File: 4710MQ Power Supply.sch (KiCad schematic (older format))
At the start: 20 parts, among them J1 Jack-DC, J2 ATX 4 Pin, J3 Molex 4 Pin, U1 MP1499GD-Z

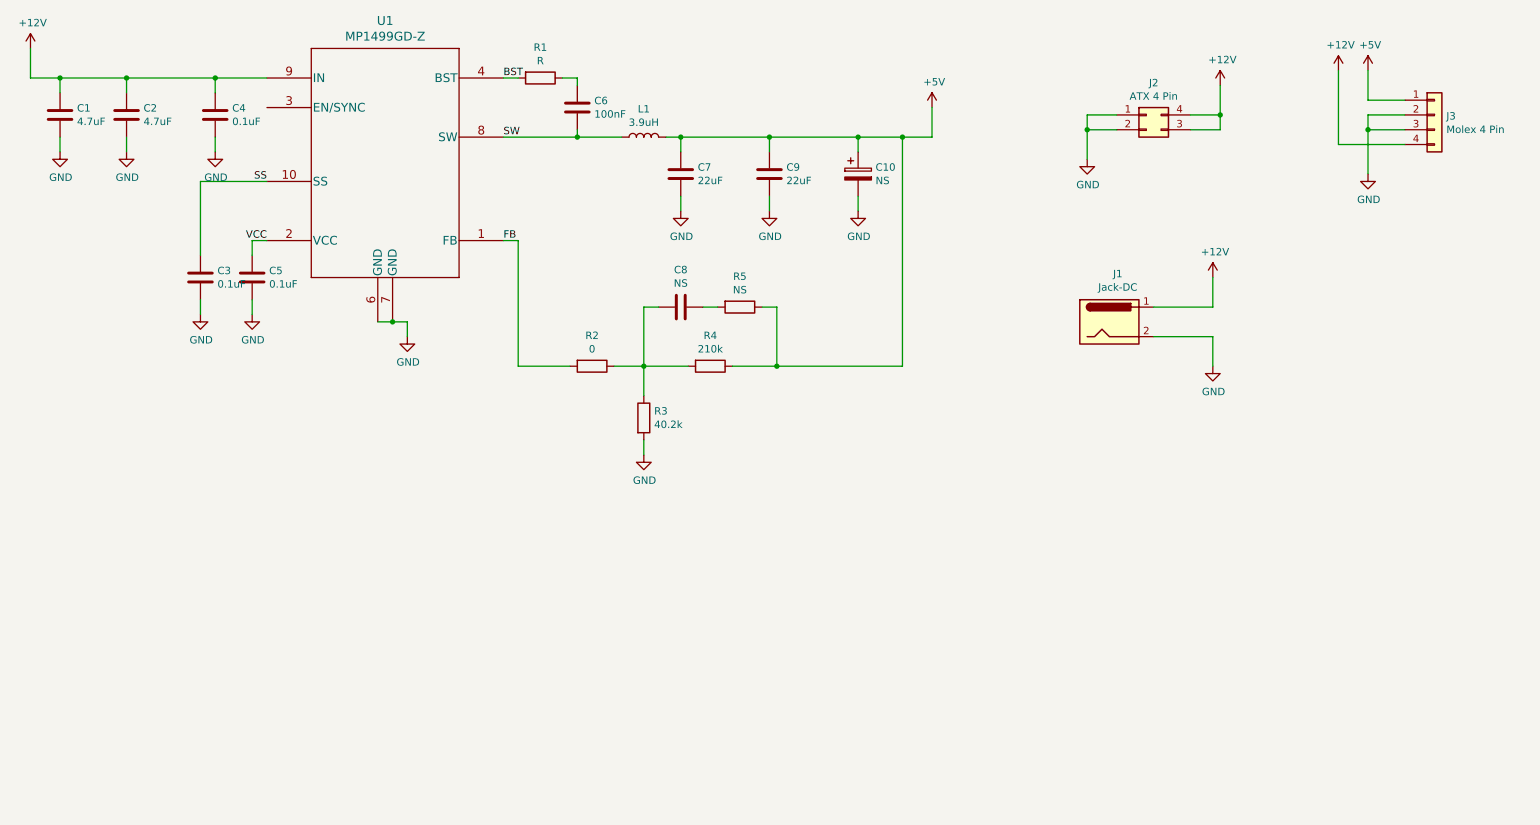
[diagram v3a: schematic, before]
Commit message: Version 3.0
- Added Current Sensor
- Added Thermometer IC
- Added 2.54 pitch 4pin output
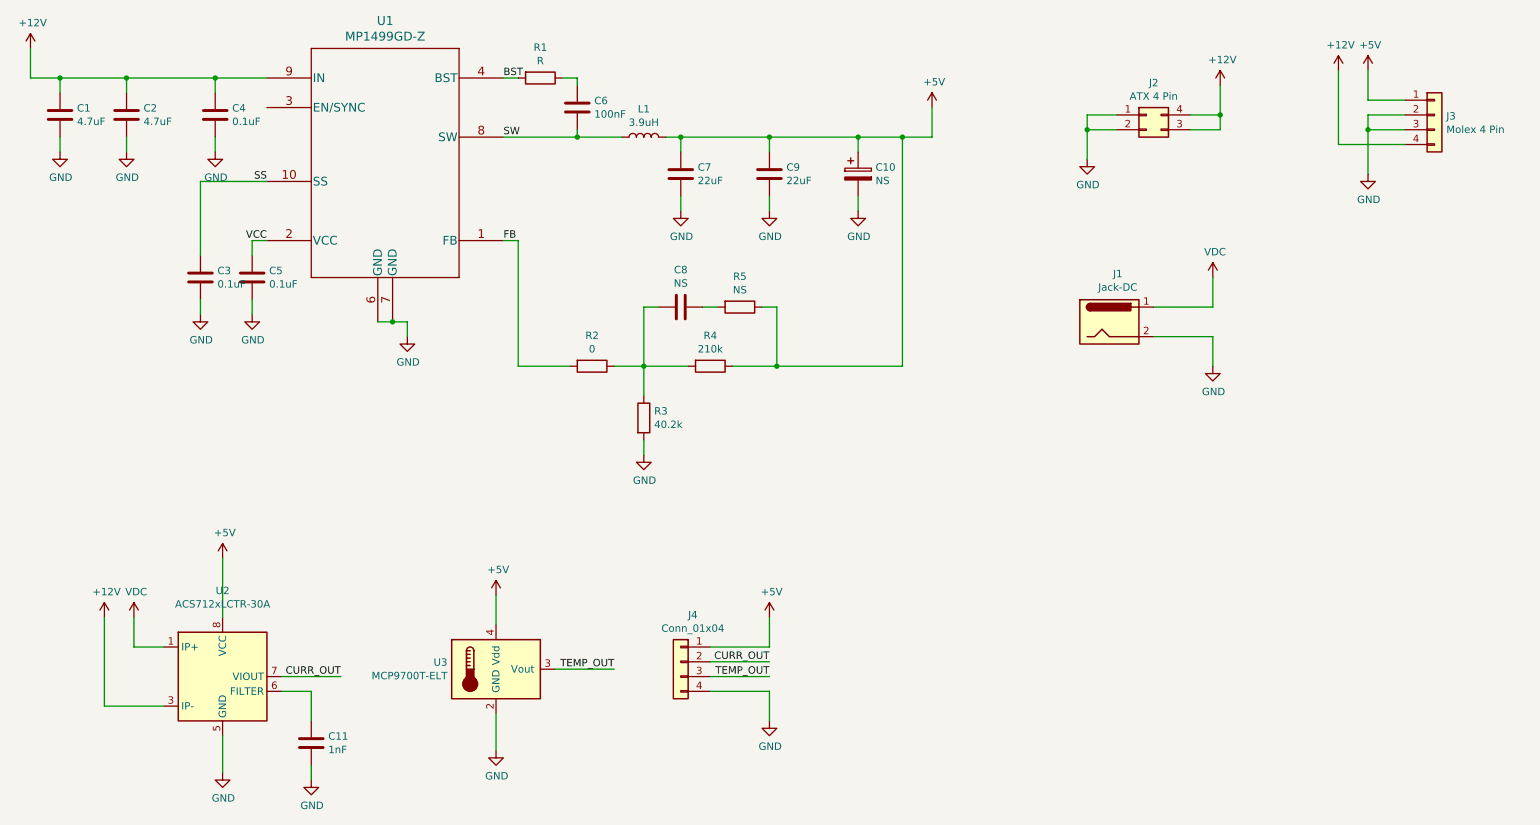
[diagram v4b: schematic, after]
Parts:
- added C11: 1nF, Capacitor_SMD:C_0805_2012Metric_Pad1.18x1.45mm_HandSolder, symbol Device:C
- added J4: Conn_01x04, Connector_PinSocket_2.54mm:PinSocket_1x04_P2.54mm_Vertical, symbol Connector_Generic:Conn_01x04
- added U2: ACS712xLCTR-30A, Package_SO:SOIC-8_3.9x4.9mm_P1.27mm, symbol Sensor_Current:ACS712xLCTR-30A
- added U3: MCP9700T-ELT, Package_TO_SOT_SMD:SOT-353_SC-70-5, symbol Sensor_Temperature:MCP9700T-ELT
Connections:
- net +12V: now also U2.3 (IP-), U2.4 (IP-); no longer J1.1
- net +5V: now also J4.1 (Pin_1), U2.8 (VCC), U3.4 (Vdd)
- net GND: now also C11.2, J4.4 (Pin_4), U2.5 (GND), U3.2 (GND)
- new net: C11.1, U2.6 (FILTER)
- new net CURR_OUT: J4.2 (Pin_2), U2.7 (VIOUT)
- new net TEMP_OUT: J4.3 (Pin_3), U3.3 (Vout)
- new net VDC: J1.1, U2.1 (IP+), U2.2 (IP+)
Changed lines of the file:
@@
 $EndComp
 $Comp
-L power:+12V #PWR0101
-U 1 1 614C8ABC
-P 8700 2550
-F 0 "#PWR0101" H 8700 2400 50  0001 C CNN
-F 1 "+12V" H 8715 2723 50  0000 C CNN
-F 2 "" H 8700 2550 50  0001 C CNN
-F 3 "" H 8700 2550 50  0001 C CNN
-	1    8700 2550
-	1    0    0    -1
-$EndComp
-$Comp
-L power:GND #PWR?
+L power:GND #PWR0101
 U 1 1 614CA392
 P 4850 3750
-F 0 "#PWR?" H 4850 3500 50  0001 C CNN
+F 0 "#PWR0101" H 4850 3500 50  0001 C CNN
 F 1 "GND" H 4855 3577 50  0000 C CNN
 F 2 "" H 4850 3750 50  0001 C CNN
@@
 	1    0    0    -1
 $EndComp
+$Comp
+L Sensor_Current:ACS712xLCTR-30A U2
+U 1 1 614D05D1
+P 2000 5250
+F 0 "U2" H 2000 5831 50  0000 C CNN
+F 1 "ACS712xLCTR-30A" H 2000 5740 50  0000 C CNN
+F 2 "Package_SO:SOIC-8_3.9x4.9mm_P1.27mm" H 2100 4900 50  0001 L CIN
+F 3 "http://www.allegromicro.com/~/media/Files/Datasheets/ACS712-Datasheet.ashx?la=en" H 2000 5250 50  0001 C CNN
+	1    2000 5250
+	1    0    0    -1
+$EndComp
+Wire Wire Line
+	1600 5050 1400 5050
+Wire Wire Line
+	1400 5050 1400 4850
+Wire Wire Line
+	1600 5450 1200 5450
+Wire Wire Line
+	1200 5450 1200 4850
+$Comp
+L power:+12V #PWR0102
+U 1 1 614D6643
+P 1200 4850
+F 0 "#PWR0102" H 1200 4700 50  0001 C CNN
+F 1 "+12V" H 1215 5023 50  0000 C CNN
+F 2 "" H 1200 4850 50  0001 C CNN
+F 3 "" H 1200 4850 50  0001 C CNN
+	1    1200 4850
+	1    0    0    -1
+$EndComp
+$Comp
+L power:VDC #PWR0103
+U 1 1 614D6B25
+P 1400 4850
+F 0 "#PWR0103" H 1400 4750 50  0001 C CNN
+F 1 "VDC" H 1415 5023 50  0000 C CNN
+F 2 "" H 1400 4850 50  0001 C CNN
+F 3 "" H 1400 4850 50  0001 C CNN
+	1    1400 4850
+	1    0    0    -1
+$EndComp
+$Comp
+L power:VDC #PWR0104
+U 1 1 614D6F1F
+P 8700 2550
+F 0 "#PWR0104" H 8700 2450 50  0001 C CNN
+F 1 "VDC" H 8715 2723 50  0000 C CNN
+F 2 "" H 8700 2550 50  0001 C CNN
+F 3 "" H 8700 2550 50  0001 C CNN
+	1    8700 2550
+	1    0    0    -1
+$EndComp
+Wire Wire Line
+	2000 4450 2000 4850
+$Comp
+L power:+5V #PWR0105
+U 1 1 614DC640
+P 2000 4450
+F 0 "#PWR0105" H 2000 4300 50  0001 C CNN
+F 1 "+5V" H 2015 4623 50  0000 C CNN
+F 2 "" H 2000 4450 50  0001 C CNN
+F 3 "" H 2000 4450 50  0001 C CNN
+	1    2000 4450
+	1    0    0    -1
+$EndComp
+Wire Wire Line
+	2000 5650 2000 5900
+$Comp
+L power:GND #PWR0106
+U 1 1 614DE695
+P 2000 5900
+F 0 "#PWR0106" H 2000 5650 50  0001 C CNN
+F 1 "GND" H 2005 5727 50  0000 C CNN
+F 2 "" H 2000 5900 50  0001 C CNN
+F 3 "" H 2000 5900 50  0001 C CNN
+	1    2000 5900
+	1    0    0    -1
+$EndComp
+Wire Wire Line
+	2400 5350 2600 5350
+Wire Wire Line
+	2600 5350 2600 5550
+$Comp
+L Device:C C11
+U 1 1 614E0AE1
+P 2600 5700
+F 0 "C11" H 2715 5746 50  0000 L CNN
+F 1 "1nF" H 2715 5655 50  0000 L CNN
+F 2 "Capacitor_SMD:C_0805_2012Metric_Pad1.18x1.45mm_HandSolder" H 2638 5550 50  0001 C CNN
+F 3 "~" H 2600 5700 50  0001 C CNN
+	1    2600 5700
+	1    0    0    -1
+$EndComp
+Wire Wire Line
+	2600 5850 2600 5950
+$Comp
+L power:GND #PWR0107
+U 1 1 614E305D
+P 2600 5950
+F 0 "#PWR0107" H 2600 5700 50  0001 C CNN
+F 1 "GND" H 2605 5777 50  0000 C CNN
+F 2 "" H 2600 5950 50  0001 C CNN
+F 3 "" H 2600 5950 50  0001 C CNN
+	1    2600 5950
+	1    0    0    -1
+$EndComp
+Wire Wire Line
+	2400 5250 2800 5250
+Text Label 2800 5250 2    50   ~ 0
+CURR_OUT
+Wire Wire Line
+	5300 5050 5700 5050
+Wire Wire Line
+	5300 5150 5700 5150
+Wire Wire Line
+	5300 5350 5700 5350
+Wire Wire Line
+	5700 5350 5700 5550
+Wire Wire Line
+	5700 5050 5700 4850
+Text Label 5700 5150 2    50   ~ 0
+CURR_OUT
+$Comp
+L power:+5V #PWR0108
+U 1 1 614F337E
+P 5700 4850
+F 0 "#PWR0108" H 5700 4700 50  0001 C CNN
+F 1 "+5V" H 5715 5023 50  0000 C CNN
+F 2 "" H 5700 4850 50  0001 C CNN
+F 3 "" H 5700 4850 50  0001 C CNN
+	1    5700 4850
+	1    0    0    -1
+$EndComp
+$Comp
+L power:GND #PWR0109
+U 1 1 614F382B
+P 5700 5550
+F 0 "#PWR0109" H 5700 5300 50  0001 C CNN
+F 1 "GND" H 5705 5377 50  0000 C CNN
+F 2 "" H 5700 5550 50  0001 C CNN
+F 3 "" H 5700 5550 50  0001 C CNN
+	1    5700 5550
+	1    0    0    -1
+$EndComp
+$Comp
+L Sensor_Temperature:MCP9700T-ELT U3
+U 1 1 6150CABE
+P 3850 5200
+F 0 "U3" H 3521 5246 50  0000 R CNN
+F 1 "MCP9700T-ELT" H 3521 5155 50  0000 R CNN
+F 2 "Package_TO_SOT_SMD:SOT-353_SC-70-5" H 3850 4800 50  0001 C CNN
+F 3 "http://ww1.microchip.com/downloads/en/DeviceDoc/21942e.pdf" H 3850 5200 50  0001 C CNN
+	1    3850 5200
+	1    0    0    -1
+$EndComp
+$Comp
+L Connector_Generic:Conn_01x04 J4
+U 1 1 6150F647
+P 5100 5150
+F 0 "J4" H 5018 5467 50  0000 C CNN
+F 1 "Conn_01x04" H 5018 5376 50  0000 C CNN
+F 2 "Connector_PinSocket_2.54mm:PinSocket_1x04_P2.54mm_Vertical" H 5100 5150 50  0001 C CNN
+F 3 "~" H 5100 5150 50  0001 C CNN
+	1    5100 5150
+	-1   0    0    -1
+$EndComp
+Wire Wire Line
+	5300 5250 5700 5250
+Text Label 5700 5250 2    50   ~ 0
+TEMP_OUT
+Wire Wire Line
+	3850 4900 3850 4700
+Wire Wire Line
+	3850 5500 3850 5750
+Wire Wire Line
+	4250 5200 4650 5200
+Text Label 4650 5200 2    50   ~ 0
+TEMP_OUT
+$Comp
+L power:+5V #PWR0110
+U 1 1 61530D8E
+P 3850 4700
+F 0 "#PWR0110" H 3850 4550 50  0001 C CNN
+F 1 "+5V" H 3865 4873 50  0000 C CNN
+F 2 "" H 3850 4700 50  0001 C CNN
+F 3 "" H 3850 4700 50  0001 C CNN
+	1    3850 4700
+	1    0    0    -1
+$EndComp
+$Comp
+L power:GND #PWR0111
+U 1 1 61531296
+P 3850 5750
+F 0 "#PWR0111" H 3850 5500 50  0001 C CNN
+F 1 "GND" H 3855 5577 50  0000 C CNN
+F 2 "" H 3850 5750 50  0001 C CNN
+F 3 "" H 3850 5750 50  0001 C CNN
+	1    3850 5750
+	1    0    0    -1
+$EndComp
